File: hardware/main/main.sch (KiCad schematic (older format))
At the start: 2 parts, among them J101 Conn_01x11_Male, J102 Conn_01x11_Male

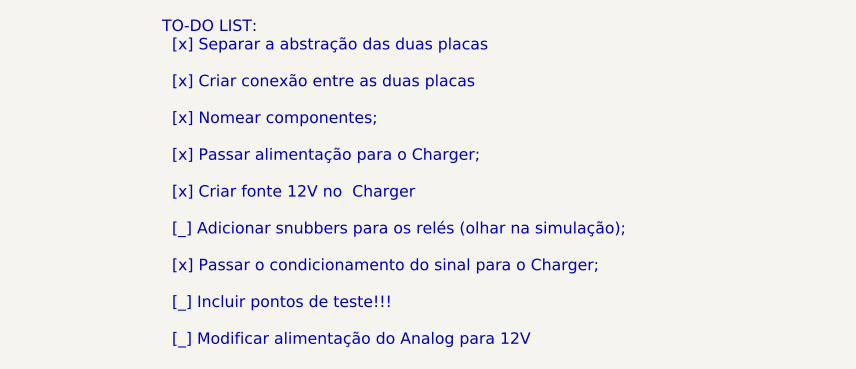
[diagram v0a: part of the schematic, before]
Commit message: Esquematico primeira versão Erro de referencia dos componentes na PCB com os do Esquematico solucionados
Pontos de teste adicionados
Alimentar o analog com +12V
Adicionar Snubber para os reles
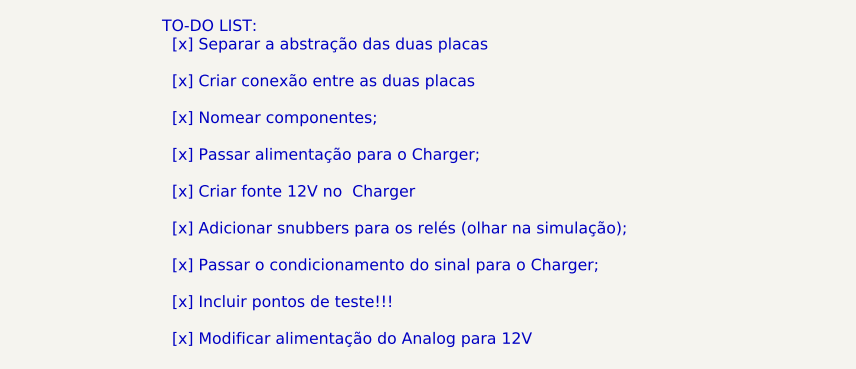
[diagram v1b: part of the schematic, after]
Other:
- note added: "TO-DO LIST:\n [x] Separar a abstração das duas placas\n\n [x] Criar conexão entre as duas placas\n\n [x] Nomear componentes;\n\n [x] Passar alimentação para o Charger;\n\n [x] Criar fonte 12V no Charger\n\n [x] Adicionar snubbers para os relés (olhar na simulação);\n\n [x] Passar o condicionamento do sinal para o Charger;\n\n [x] Incluir pontos de teste!!!\n\n [x] Modificar alimentação do Analog 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"
- note removed: "TO-DO LIST:\n [x] Separar a abstração das duas placas\n\n [x] Criar conexão entre as duas placas\n\n [x] Nomear componentes;\n\n [x] Passar alimentação para o Charger;\n\n [x] Criar fonte 12V no Charger\n\n [_] Adicionar snubbers para os relés (olhar na simulação);\n\n [x] Passar o condicionamento do sinal para o Charger;\n\n [_] Incluir pontos de teste!!!\n\n [_] Modificar alimentação do Analog 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"
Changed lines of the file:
@@
 EESchema Schematic File Version 4
 LIBS:main-cache
-EELAYER 29 0
+EELAYER 26 0
 EELAYER END
 $Descr A4 11693 8268
@@
 Connection ~ 4400 3150
 Text Notes 4450 5600 0    50   ~ 0
-TO-DO LIST:\n  [x] Separar a abstração das duas placas\n\n  [x] Criar conexão entre as duas placas\n\n  [x] Nomear componentes;\n\n  [x] Passar alimentação para o Charger;\n\n  [x] Criar fonte 12V no  Charger\n\n  [_] Adicionar snubbers para os relés (olhar na simulação);\n\n  [x] Passar o condicionamento do sinal para o Charger;\n\n  [_] Incluir pontos de teste!!!\n\n  [_] Modificar alimentação do Analog para 12V
+TO-DO LIST:\n  [x] Separar a abstração das duas placas\n\n  [x] Criar conexão entre as duas placas\n\n  [x] Nomear componentes;\n\n  [x] Passar alimentação para o Charger;\n\n  [x] Criar fonte 12V no  Charger\n\n  [x] Adicionar snubbers para os relés (olhar na simulação);\n\n  [x] Passar o condicionamento do sinal para o Charger;\n\n  [x] Incluir pontos de teste!!!\n\n  [x] Modificar alimentação do Analog para 12V
 Wire Wire Line
 	4350 2950 4250 2950

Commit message: Footprints
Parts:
- J101, J102: footprint (none) -> KicadZeniteSolarLibrary18:PinHeader_1x11_P2.54mm_Vertical_HandSoldering
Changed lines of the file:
@@
 F 0 "J101" H 5000 3950 50  0000 R CNN
 F 1 "Conn_01x11_Male" H 5000 3850 50  0000 R CNN
-F 2 "" H 4700 3250 50  0001 C CNN
+F 2 "KicadZeniteSolarLibrary18:PinHeader_1x11_P2.54mm_Vertical_HandSoldering" H 4700 3250 50  0001 C CNN
 F 3 "~" H 4700 3250 50  0001 C CNN
 	1    4700 3250
@@
 F 0 "J102" H 5850 3950 50  0000 R CNN
 F 1 "Conn_01x11_Male" H 5850 3850 50  0000 R CNN
-F 2 "" H 5550 3250 50  0001 C CNN
+F 2 "KicadZeniteSolarLibrary18:PinHeader_1x11_P2.54mm_Vertical_HandSoldering" H 5550 3250 50  0001 C CNN
 F 3 "~" H 5550 3250 50  0001 C CNN
 	1    5550 3250

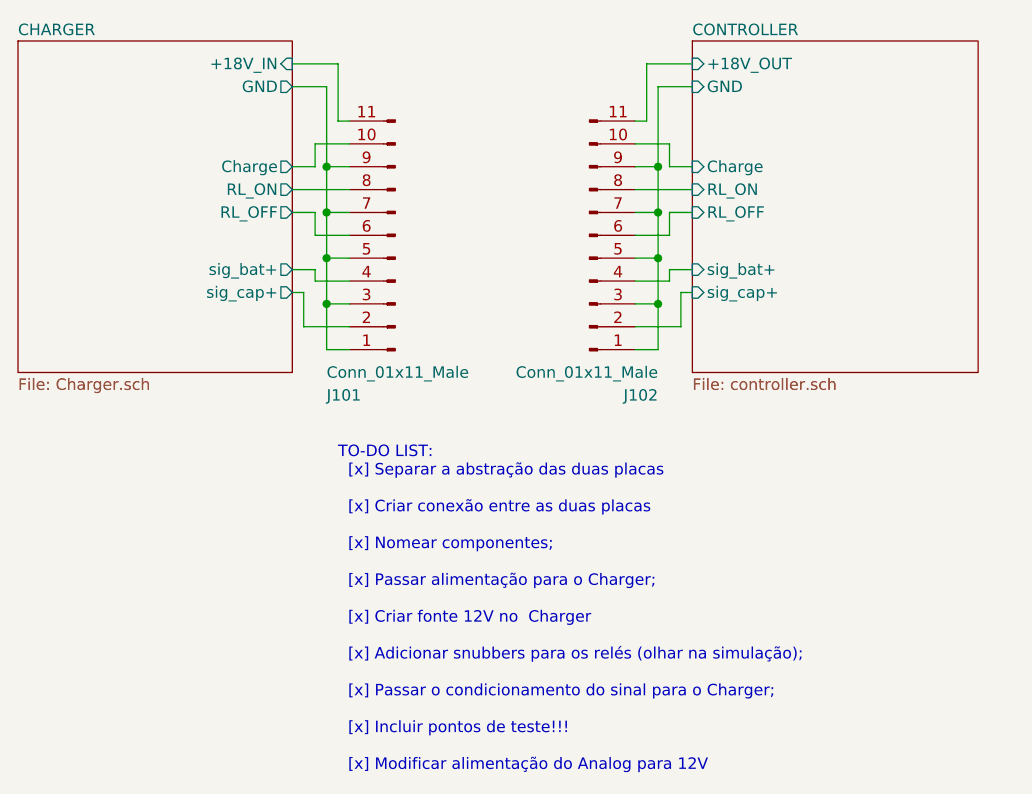
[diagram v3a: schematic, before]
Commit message: Layout and Relay footprint
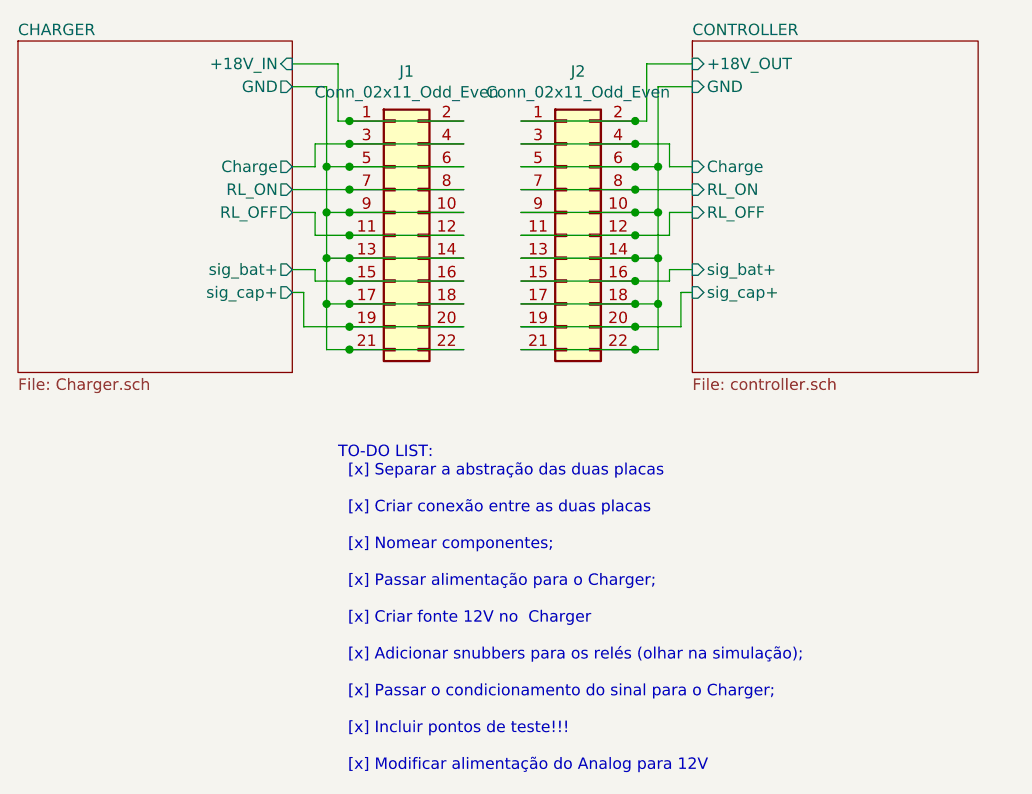
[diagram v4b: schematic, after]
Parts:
- removed J101, J102: Conn_01x11_Male, KicadZeniteSolarLibrary18:PinHeader_1x11_P2.54mm_Vertical_HandSoldering, symbol Connector:Conn_01x11_Male
- added J1, J2: Conn_02x11_Odd_Even, KicadZeniteSolarLibrary18:PinHeader_2x11_P2.54mm_Vertical_HandSoldering, symbol Connector_Generic:Conn_02x11_Odd_Even
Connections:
- net CHARGER/+18V_IN: now also J1.1 (Pin_1), J1.2 (Pin_2)
- net CHARGER/Charge: now also J1.3 (Pin_3), J1.4 (Pin_4)
- net CHARGER/GND: now also J1.10 (Pin_10), J1.13 (Pin_13), J1.14 (Pin_14), J1.17 (Pin_17), J1.18 (Pin_18), J1.21 (Pin_21), J1.22 (Pin_22), J1.5 (Pin_5), J1.6 (Pin_6), J1.9 (Pin_9)
- net CHARGER/RL_OFF: now also J1.11 (Pin_11), J1.12 (Pin_12)
- net CHARGER/RL_ON: now also J1.7 (Pin_7), J1.8 (Pin_8)
- net CHARGER/sig_bat+: now also J1.15 (Pin_15), J1.16 (Pin_16)
- net CHARGER/sig_cap+: now also J1.19 (Pin_19), J1.20 (Pin_20)
- net CONTROLLER/+18V_OUT: now also J2.1 (Pin_1), J2.2 (Pin_2)
- net CONTROLLER/Charge: now also J2.3 (Pin_3), J2.4 (Pin_4)
- net CONTROLLER/GND: now also J2.10 (Pin_10), J2.13 (Pin_13), J2.14 (Pin_14), J2.17 (Pin_17), J2.18 (Pin_18), J2.21 (Pin_21), J2.22 (Pin_22), J2.5 (Pin_5), J2.6 (Pin_6), J2.9 (Pin_9)
- net CONTROLLER/RL_OFF: now also J2.11 (Pin_11), J2.12 (Pin_12)
- net CONTROLLER/RL_ON: now also J2.7 (Pin_7), J2.8 (Pin_8)
- net CONTROLLER/sig_bat+: now also J2.15 (Pin_15), J2.16 (Pin_16)
- net CONTROLLER/sig_cap+: now also J2.19 (Pin_19), J2.20 (Pin_20)
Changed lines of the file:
@@
 F8 "sig_cap+" I L 6000 3500 50
 $EndSheet
+Wire Wire Line
+	4250 3150 4350 3150
+Wire Wire Line
+	4350 2950 4350 2850
+Wire Wire Line
+	4350 2850 4500 2850
+Wire Wire Line
+	4250 3050 4500 3050
+Wire Wire Line
+	4350 3150 4350 3250
+Wire Wire Line
+	4400 3150 4500 3150
+Text Notes 4450 5600 0    50   ~ 0
+TO-DO LIST:\n  [x] Separar a abstração das duas placas\n\n  [x] Criar conexão entre as duas placas\n\n  [x] Nomear componentes;\n\n  [x] Passar alimentação para o Charger;\n\n  [x] Criar fonte 12V no  Charger\n\n  [x] Adicionar snubbers para os relés (olhar na simulação);\n\n  [x] Passar o condicionamento do sinal para o Charger;\n\n  [x] Incluir pontos de teste!!!\n\n  [x] Modificar alimentação do Analog para 12V
+Wire Wire Line
+	4350 2950 4250 2950
+Wire Wire Line
+	4250 2600 4400 2600
+Wire Wire Line
+	4250 2500 4450 2500
+Wire Wire Line
+	4450 2500 4450 2750
+Wire Wire Line
+	4400 3750 4500 3750
+Wire Wire Line
+	4400 3350 4500 3350
+Wire Wire Line
+	4500 3450 4350 3450
+Wire Wire Line
+	4350 3450 4350 3400
+Wire Wire Line
+	4350 3400 4250 3400
+Wire Wire Line
+	4250 3500 4300 3500
+Wire Wire Line
+	4300 3500 4300 3650
+Wire Wire Line
+	4300 3650 4500 3650
+Wire Wire Line
+	6000 3150 5900 3150
+Wire Wire Line
+	5850 2950 5850 3150
+Wire Wire Line
+	5850 3150 5850 3350
+Connection ~ 5850 3150
+Wire Wire Line
+	5900 2950 6000 2950
+Wire Wire Line
+	6000 2600 5850 2600
+Wire Wire Line
+	5850 2600 5850 2950
+Connection ~ 5850 2950
+Wire Wire Line
+	6000 2500 5800 2500
+Wire Wire Line
+	5800 2500 5800 2750
+Wire Wire Line
+	5850 3350 5850 3550
+Connection ~ 5850 3350
+Wire Wire Line
+	5850 3550 5850 3750
+Connection ~ 5850 3550
+Wire Wire Line
+	5900 3450 5900 3400
+Wire Wire Line
+	5900 3400 6000 3400
+Wire Wire Line
+	6000 3500 5950 3500
+Wire Wire Line
+	5950 3500 5950 3650
 $Comp
-L Connector:Conn_01x11_Male J101
-U 1 1 5CA76C06
+L Connector_Generic:Conn_02x11_Odd_Even J1
+U 1 1 5CA976F8
 P 4700 3250
-F 0 "J101" H 5000 3950 50  0000 R CNN
-F 1 "Conn_01x11_Male" H 5000 3850 50  0000 R CNN
-F 2 "KicadZeniteSolarLibrary18:PinHeader_1x11_P2.54mm_Vertical_HandSoldering" H 4700 3250 50  0001 C CNN
+F 0 "J1" H 4750 3967 50  0000 C CNN
+F 1 "Conn_02x11_Odd_Even" H 4750 3876 50  0000 C CNN
+F 2 "KicadZeniteSolarLibrary18:PinHeader_2x11_P2.54mm_Vertical_HandSoldering" H 4700 3250 50  0001 C CNN
 F 3 "~" H 4700 3250 50  0001 C CNN
 	1    4700 3250
-	-1   0    0    1
+	1    0    0    -1
 $EndComp
 Wire Wire Line
-	4250 3150 4350 3150
-Wire Wire Line
-	4350 2950 4350 2850
-Wire Wire Line
-	4350 2850 4500 2850
-Wire Wire Line
-	4250 3050 4500 3050
-Wire Wire Line
-	4350 3150 4350 3250
+	4450 2750 4500 2750
+Wire Wire Line
+	5000 2750 4500 2750
+Connection ~ 4500 2750
+Connection ~ 4500 2850
+Wire Wire Line
+	4400 2950 4500 2950
+Connection ~ 4500 2950
+Connection ~ 4500 3050
+Wire Wire Line
+	5000 3150 4500 3150
+Connection ~ 4500 3150
 Wire Wire Line
 	4350 3250 4500 3250
-Wire Wire Line
-	4500 2950 4400 2950
+Connection ~ 4500 3250
+Wire Wire Line
+	5000 3350 4500 3350
+Connection ~ 4500 3350
+Connection ~ 4500 3450
+Wire Wire Line
+	4400 3550 4500 3550
+Connection ~ 4500 3550
+Connection ~ 4500 3650
+Wire Wire Line
+	5000 3750 4500 3750
+Connection ~ 4500 3750
+Wire Wire Line
+	5000 3650 4500 3650
+Wire Wire Line
+	5000 3050 4500 3050
+Wire Wire Line
+	5000 3450 4500 3450
+Wire Wire Line
+	5850 3750 5750 3750
+Wire Wire Line
+	4500 3550 5000 3550
+Wire Wire Line
+	5800 2750 5750 2750
+Wire Wire Line
+	4500 2950 5000 2950
+Wire Wire Line
+	4500 3250 5000 3250
+Wire Wire Line
+	5900 3250 5750 3250
+Wire Wire Line
+	5000 2850 4500 2850
+Connection ~ 4400 3550
+Connection ~ 4400 3350
+Wire Wire Line
+	4400 3550 4400 3750
+Wire Wire Line
+	4400 3350 4400 3550
+Connection ~ 4400 2950
+Wire Wire Line
+	4400 2600 4400 2950
+Connection ~ 4400 3150
+Wire Wire Line
+	4400 3150 4400 3350
 Wire Wire Line
 	4400 2950 4400 3150
 Wire Wire Line
-	4400 3150 4500 3150
-Wire Wire Line
-	4400 3150 4400 3350
-Connection ~ 4400 3150
-Text Notes 4450 5600 0    50   ~ 0
-TO-DO LIST:\n  [x] Separar a abstração das duas placas\n\n  [x] Criar conexão entre as duas placas\n\n  [x] Nomear componentes;\n\n  [x] Passar alimentação para o Charger;\n\n  [x] Criar fonte 12V no  Charger\n\n  [x] Adicionar snubbers para os relés (olhar na simulação);\n\n  [x] Passar o condicionamento do sinal para o Charger;\n\n  [x] Incluir pontos de teste!!!\n\n  [x] Modificar alimentação do Analog para 12V
-Wire Wire Line
-	4350 2950 4250 2950
-Wire Wire Line
-	4250 2600 4400 2600
-Wire Wire Line
-	4400 2600 4400 2950
-Connection ~ 4400 2950
-Wire Wire Line
-	4250 2500 4450 2500
-Wire Wire Line
-	4450 2500 4450 2750
-Wire Wire Line
-	4450 2750 4500 2750
-Wire Wire Line
-	4400 3350 4400 3550
-Wire Wire Line
-	4400 3550 4500 3550
-Connection ~ 4400 3350
-Wire Wire Line
-	4400 3550 4400 3750
-Wire Wire Line
-	4400 3750 4500 3750
-Wire Wire Line
-	4400 3350 4500 3350
-Connection ~ 4400 3550
-Wire Wire Line
-	4500 3450 4350 3450
-Wire Wire Line
-	4350 3450 4350 3400
-Wire Wire Line
-	4350 3400 4250 3400
-Wire Wire Line
-	4250 3500 4300 3500
-Wire Wire Line
-	4300 3500 4300 3650
-Wire Wire Line
-	4300 3650 4500 3650
+	5900 2950 5900 2850
+Wire Wire Line
+	5900 3150 5900 3250
 $Comp
-L Connector:Conn_01x11_Male J102
-U 1 1 5CBD36A2
-P 5550 3250
-F 0 "J102" H 5850 3950 50  0000 R CNN
-F 1 "Conn_01x11_Male" H 5850 3850 50  0000 R CNN
-F 2 "KicadZeniteSolarLibrary18:PinHeader_1x11_P2.54mm_Vertical_HandSoldering" H 5550 3250 50  0001 C CNN
-F 3 "~" H 5550 3250 50  0001 C CNN
-	1    5550 3250
-	1    0    0    1
+L Connector_Generic:Conn_02x11_Odd_Even J2
+U 1 1 5CAAC328
+P 5450 3250
+F 0 "J2" H 5500 3967 50  0000 C CNN
+F 1 "Conn_02x11_Odd_Even" H 5500 3876 50  0000 C CNN
+F 2 "KicadZeniteSolarLibrary18:PinHeader_2x11_P2.54mm_Vertical_HandSoldering" H 5450 3250 50  0001 C CNN
+F 3 "~" H 5450 3250 50  0001 C CNN
+	1    5450 3250
+	1    0    0    -1
 $EndComp
 Wire Wire Line
-	6000 3150 5900 3150
-Wire Wire Line
-	5900 2950 5900 2850
-Wire Wire Line
-	5900 2850 5750 2850
-Wire Wire Line
-	6000 3050 5750 3050
-Wire Wire Line
-	5900 3150 5900 3250
-Wire Wire Line
-	5900 3250 5750 3250
+	5250 2750 5750 2750
+Connection ~ 5750 2750
+Wire Wire Line
+	5250 2850 5750 2850
+Connection ~ 5750 2850
+Wire Wire Line
+	5750 2850 5900 2850
+Wire Wire Line
+	5250 2950 5750 2950
+Connection ~ 5750 2950
 Wire Wire Line
 	5750 2950 5850 2950
 Wire Wire Line
-	5850 2950 5850 3150
-Wire Wire Line
-	5850 3150 5750 3150
-Wire Wire Line
-	5850 3150 5850 3350
-Connection ~ 5850 3150
-Wire Wire Line
-	5900 2950 6000 2950
-Wire Wire Line
-	6000 2600 5850 2600
-Wire Wire Line
-	5850 2600 5850 2950
-Connection ~ 5850 2950
-Wire Wire Line
-	6000 2500 5800 2500
-Wire Wire Line
-	5800 2500 5800 2750
-Wire Wire Line
-	5800 2750 5750 2750
-Wire Wire Line
-	5850 3350 5850 3550
-Wire Wire Line
-	5850 3550 5750 3550
-Connection ~ 5850 3350
-Wire Wire Line
-	5850 3550 5850 3750
-Wire Wire Line
-	5850 3750 5750 3750
-Wire Wire Line
-	5850 3350 5750 3350
-Connection ~ 5850 3550
+	5250 3050 5750 3050
+Connection ~ 5750 3050
+Wire Wire Line
+	5750 3050 6000 3050
+Wire Wire Line
+	5250 3150 5750 3150
+Connection ~ 5750 3150
+Wire Wire Line
+	5750 3150 5850 3150
+Wire Wire Line
+	5250 3250 5750 3250
+Connection ~ 5750 3250
+Wire Wire Line
+	5250 3350 5750 3350
+Connection ~ 5750 3350
+Wire Wire Line
+	5750 3350 5850 3350
+Wire Wire Line
+	5250 3450 5750 3450
+Connection ~ 5750 3450
 Wire Wire Line
 	5750 3450 5900 3450
 Wire Wire Line
-	5900 3450 5900 3400
-Wire Wire Line
-	5900 3400 6000 3400
-Wire Wire Line
-	6000 3500 5950 3500
-Wire Wire Line
-	5950 3500 5950 3650
-Wire Wire Line
-	5950 3650 5750 3650
+	5250 3550 5750 3550
+Connection ~ 5750 3550
+Wire Wire Line
+	5750 3550 5850 3550
+Wire Wire Line
+	5250 3650 5750 3650
+Connection ~ 5750 3650
+Wire Wire Line
+	5750 3650 5950 3650
+Wire Wire Line
+	5250 3750 5750 3750
+Connection ~ 5750 3750
 $EndSCHEMATC

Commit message: Ampop layout not finished
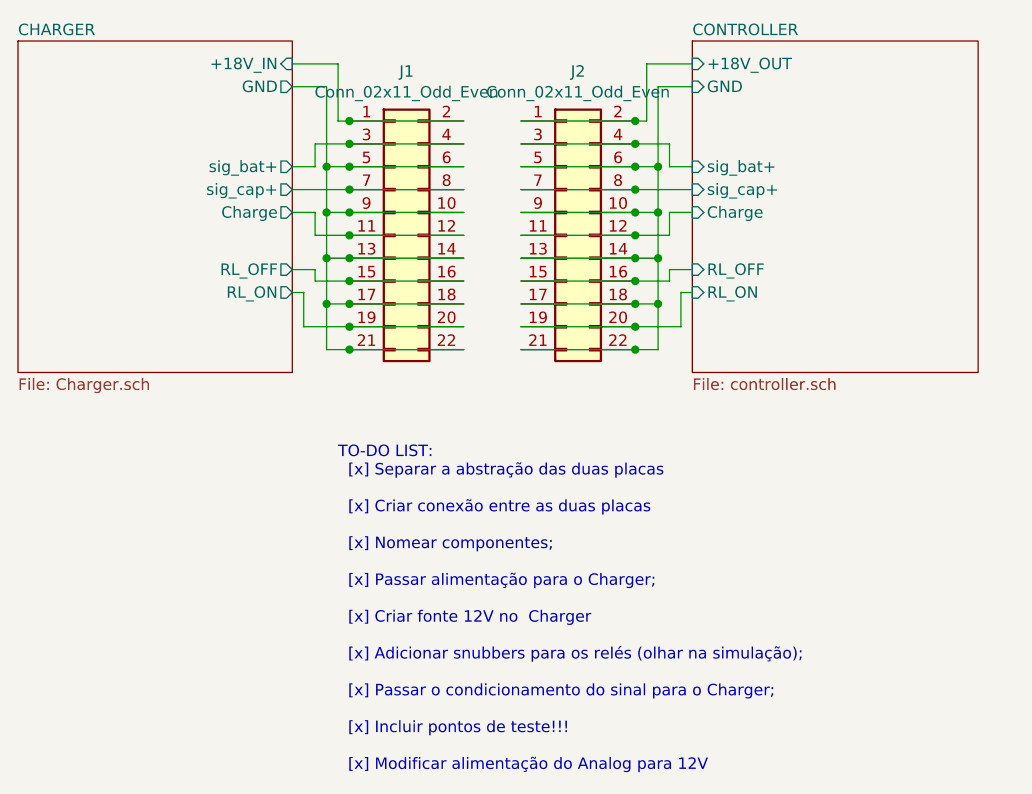
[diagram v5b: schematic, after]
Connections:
- net CHARGER/Charge: now also J1.11 (Pin_11), J1.12 (Pin_12); no longer J1.3 (Pin_3), J1.4 (Pin_4)
- net CHARGER/RL_OFF: now also J1.15 (Pin_15), J1.16 (Pin_16); no longer J1.11 (Pin_11), J1.12 (Pin_12)
- net CHARGER/RL_ON: now also J1.19 (Pin_19), J1.20 (Pin_20); no longer J1.7 (Pin_7), J1.8 (Pin_8)
- net CHARGER/sig_bat+: now also J1.3 (Pin_3), J1.4 (Pin_4); no longer J1.15 (Pin_15), J1.16 (Pin_16)
- net CHARGER/sig_cap+: now also J1.7 (Pin_7), J1.8 (Pin_8); no longer J1.19 (Pin_19), J1.20 (Pin_20)
- net CONTROLLER/Charge: now also J2.11 (Pin_11), J2.12 (Pin_12); no longer J2.3 (Pin_3), J2.4 (Pin_4)
- net CONTROLLER/RL_OFF: now also J2.15 (Pin_15), J2.16 (Pin_16); no longer J2.11 (Pin_11), J2.12 (Pin_12)
- net CONTROLLER/RL_ON: now also J2.19 (Pin_19), J2.20 (Pin_20); no longer J2.7 (Pin_7), J2.8 (Pin_8)
- net CONTROLLER/sig_bat+: now also J2.3 (Pin_3), J2.4 (Pin_4); no longer J2.15 (Pin_15), J2.16 (Pin_16)
- net CONTROLLER/sig_cap+: now also J2.7 (Pin_7), J2.8 (Pin_8); no longer J2.19 (Pin_19), J2.20 (Pin_20)
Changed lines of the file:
@@
 F0 "CHARGER" 50
 F1 "Charger.sch" 50
-F2 "Charge" O R 4250 2950 50
-F3 "RL_ON" O R 4250 3050 50
-F4 "RL_OFF" O R 4250 3150 50
+F2 "Charge" O R 4250 3150 50
+F3 "RL_ON" O R 4250 3500 50
+F4 "RL_OFF" O R 4250 3400 50
 F5 "GND" O R 4250 2600 50
 F6 "+18V_IN" I R 4250 2500 50
-F7 "sig_bat+" O R 4250 3400 50
-F8 "sig_cap+" O R 4250 3500 50
+F7 "sig_bat+" O R 4250 2950 50
+F8 "sig_cap+" O R 4250 3050 50
 $EndSheet
 $Sheet
@@
 F0 "CONTROLLER" 50
 F1 "controller.sch" 50
-F2 "RL_OFF" I L 6000 3150 50
-F3 "RL_ON" I L 6000 3050 50
-F4 "Charge" I L 6000 2950 50
+F2 "RL_OFF" I L 6000 3400 50
+F3 "RL_ON" I L 6000 3500 50
+F4 "Charge" I L 6000 3150 50
 F5 "GND" I L 6000 2600 50
 F6 "+18V_OUT" I L 6000 2500 50
-F7 "sig_bat+" I L 6000 3400 50
-F8 "sig_cap+" I L 6000 3500 50
+F7 "sig_bat+" I L 6000 2950 50
+F8 "sig_cap+" I L 6000 3050 50
 $EndSheet
 Wire Wire Line

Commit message: Layout retrabalhado. Não finalizado.
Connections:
- net CHARGER/sig_bat+: now also J1.7 (Pin_7), J1.8 (Pin_8); no longer J1.3 (Pin_3), J1.4 (Pin_4)
- net CHARGER/sig_cap+: now also J1.3 (Pin_3), J1.4 (Pin_4); no longer J1.7 (Pin_7), J1.8 (Pin_8)
- net CONTROLLER/sig_bat+: now also J2.7 (Pin_7), J2.8 (Pin_8); no longer J2.3 (Pin_3), J2.4 (Pin_4)
- net CONTROLLER/sig_cap+: now also J2.3 (Pin_3), J2.4 (Pin_4); no longer J2.7 (Pin_7), J2.8 (Pin_8)
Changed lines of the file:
@@
 EESchema Schematic File Version 4
 LIBS:main-cache
-EELAYER 26 0
+EELAYER 29 0
 EELAYER END
 $Descr A4 11693 8268
@@
 F5 "GND" O R 4250 2600 50
 F6 "+18V_IN" I R 4250 2500 50
-F7 "sig_bat+" O R 4250 2950 50
-F8 "sig_cap+" O R 4250 3050 50
+F7 "sig_bat+" O R 4250 3050 50
+F8 "sig_cap+" O R 4250 2950 50
 $EndSheet
 $Sheet
@@
 F5 "GND" I L 6000 2600 50
 F6 "+18V_OUT" I L 6000 2500 50
-F7 "sig_bat+" I L 6000 2950 50
-F8 "sig_cap+" I L 6000 3050 50
+F7 "sig_bat+" I L 6000 3050 50
+F8 "sig_cap+" I L 6000 2950 50
 $EndSheet
 Wire Wire Line
